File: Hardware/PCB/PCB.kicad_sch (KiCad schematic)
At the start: 8 parts, among them J1 DC Motor Terminal, J2 Solenoid Terminal, J3 Brushless Vac Motor, J5 Brushless Pump Motor

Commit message: done with this, placed order
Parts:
- removed H3: MountingHole, MountingHole:MountingHole_3.2mm_M3, symbol Mechanical:MountingHole
- removed J1: DC Motor Terminal, Vendor_Footprints:TE_1985218, symbol Connector:Screw_Terminal_01x04
- removed J2: Solenoid Terminal, Vendor_Footprints:PHX_16PIN_1985292, symbol Connector:Screw_Terminal_01x12
- removed J3: Brushless Vac Motor, Vendor_Footprints:TE_1985205, symbol Connector:Screw_Terminal_01x03
- removed J5: Brushless Pump Motor, Vendor_Footprints:TE_1985205, symbol Connector:Screw_Terminal_01x03
- added R6, R7: 2.2k, Resistor_SMD:R_0603_1608Metric_Pad0.98x0.95mm_HandSolder, symbol Device:R_Small
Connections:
- net I2C-SCL: now also R6.2
- net I2C-SDA: now also R7.2
- new net +3.3V: R6.1, R7.1
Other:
- removed sheet rtc
- sheet brushless_motor_pwm_driver ports: added none; removed BRUSHLESS_PWM_1, BRUSHLESS_PWM_2
- sheet motor_driver ports: added none; removed MOTOR-OUT-1, MOTOR-OUT-2
- sheet motor_driver1 ports: added none; removed MOTOR-OUT-1, MOTOR-OUT-2
- sheet relay_driver ports: added none; removed COIL+, COIL-
- sheet relay_driver1 ports: added none; removed COIL+, COIL-
- sheet relay_driver2 ports: added none; removed COIL+, COIL-
- sheet relay_driver3 ports: added none; removed COIL+, COIL-
- sheet relay_driver4 ports: added none; removed COIL+, COIL-
- sheet relay_driver5 ports: added none; removed COIL+, COIL-
- sheet sensors ports: added DOUT, INPUT_MUX, PWDN, SCLK, SPEED; removed ADC_DRDY, ADC_RESET, SCL, SDA

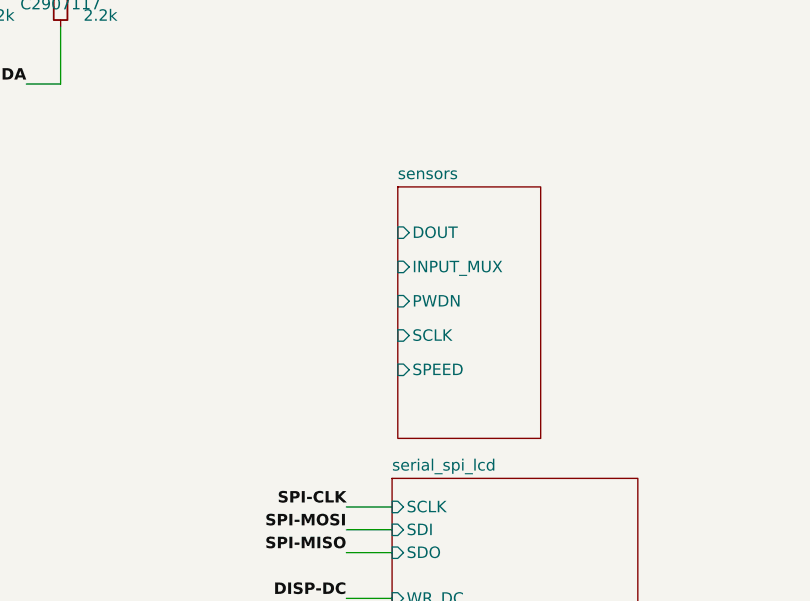
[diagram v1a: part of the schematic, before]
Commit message: fixed various hole sizes, fixed unconnected signals to ADC, pcbs have been ordered
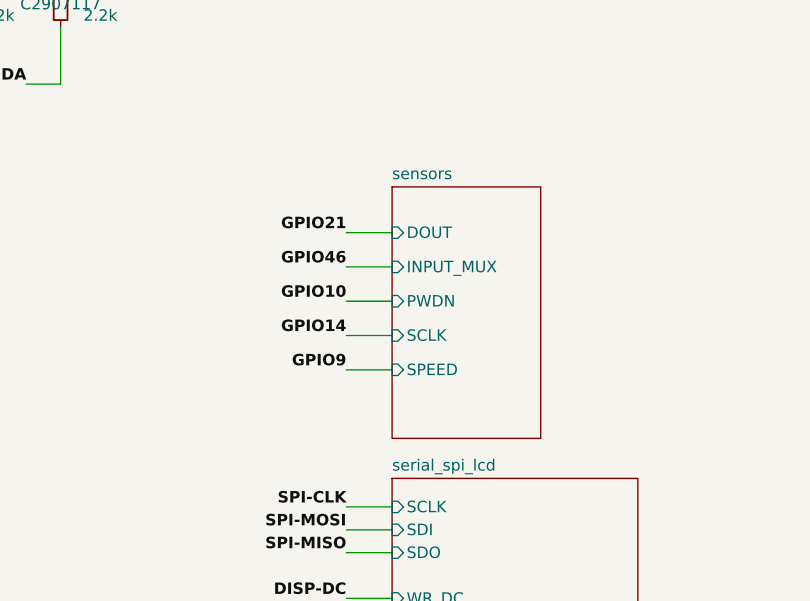
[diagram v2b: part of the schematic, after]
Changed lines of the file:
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@@
+	(wire
+		(pts
+			(xy 123.19 73.66) (xy 128.27 73.66)
+		)
+		(stroke
+			(width 0)
+			(type default)
+		)
+	)
 	(wire
 		(pts
@@
 	(wire
 		(pts
+			(xy 123.19 69.85) (xy 128.27 69.85)
+		)
+		(stroke
+			(width 0)
+			(type default)
+		)
+	)
+	(wire
+		(pts
 			(xy 191.77 109.22) (xy 198.12 109.22)
 		)
@@
 	(wire
 		(pts
+			(xy 123.19 85.09) (xy 128.27 85.09)
+		)
+		(stroke
+			(width 0)
+			(type default)
+		)
+	)
+	(wire
+		(pts
 			(xy 58.42 96.52) (xy 62.23 96.52)
 		)
@@
 	(wire
 		(pts
+			(xy 123.19 77.47) (xy 128.27 77.47)
+		)
+		(stroke
+			(width 0)
+			(type default)
+		)
+	)
+	(wire
+		(pts
 			(xy 58.42 104.14) (xy 62.23 104.14)
 		)
@@
 		(pts
 			(xy 123.19 138.43) (xy 128.27 138.43)
+		)
+		(stroke
+			(width 0)
+			(type default)
+		)
+	)
+	(wire
+		(pts
+			(xy 123.19 81.28) (xy 128.27 81.28)
 		)
 		(stroke
@@
 		)
 	)
+	(label "GPIO46"
+		(at 123.19 73.66 180)
+		(effects
+			(font
+				(size 1.27 1.27)
+				(thickness 0.254)
+				(bold yes)
+			)
+			(justify right bottom)
+		)
+	)
 	(label "DISP-BACKLIGHT"
 		(at 123.19 138.43 180)
@@
 		)
 	)
+	(label "GPIO14"
+		(at 123.19 81.28 180)
+		(effects
+			(font
+				(size 1.27 1.27)
+				(thickness 0.254)
+				(bold yes)
+			)
+			(justify right bottom)
+		)
+	)
 	(label "SOLENOID_1"
 		(at 62.23 154.94 0)
@@
 		)
 	)
+	(label "GPIO9"
+		(at 123.19 85.09 180)
+		(effects
+			(font
+				(size 1.27 1.27)
+				(thickness 0.254)
+				(bold yes)
+			)
+			(justify right bottom)
+		)
+	)
 	(label "PUMP-IN1"
 		(at 191.77 64.77 180)
@@
 		)
 	)
+	(label "GPIO21"
+		(at 123.19 69.85 180)
+		(effects
+			(font
+				(size 1.27 1.27)
+				(thickness 0.254)
+				(bold yes)
+			)
+			(justify right bottom)
+		)
+	)
 	(label "I2C-SDA"
 		(at 87.63 53.34 180)
@@
 			)
 			(justify left bottom)
+		)
+	)
+	(label "GPIO10"
+		(at 123.19 77.47 180)
+		(effects
+			(font
+				(size 1.27 1.27)
+				(thickness 0.254)
+				(bold yes)
+			)
+			(justify right bottom)
 		)
 	)
@@
 	)
 	(sheet
-		(at 128.905 64.77)
-		(size 15.875 27.94)
+		(at 128.27 64.77)
+		(size 16.51 27.94)
 		(exclude_from_sim no)
 		(in_bom yes)
@@
 		)
 		(property "Sheetname" "sensors"
-			(at 128.905 64.0584 0)
+			(at 128.27 64.0584 0)
 			(effects
 				(font
@@
 		)
 		(property "Sheetfile" "sensors.kicad_sch"
-			(at 128.905 93.2946 0)
+			(at 128.27 93.2946 0)
 			(effects
 				(font
@@
 		)
 		(pin "DOUT" input
-			(at 128.905 69.85 180)
+			(at 128.27 69.85 180)
 			(effects
 				(font
@@
 		)
 		(pin "INPUT_MUX" input
-			(at 128.905 73.66 180)
+			(at 128.27 73.66 180)
 			(effects
 				(font
@@
 		)
 		(pin "PWDN" input
-			(at 128.905 77.47 180)
+			(at 128.27 77.47 180)
 			(effects
 				(font
@@
 		)
 		(pin "SCLK" input
-			(at 128.905 81.28 180)
+			(at 128.27 81.28 180)
 			(effects
 				(font
@@
 		)
 		(pin "SPEED" input
-			(at 128.905 85.09 180)
-			(effects
-				(font
+			(at 128.27 85.09 180)
+			(effects
+				(font
